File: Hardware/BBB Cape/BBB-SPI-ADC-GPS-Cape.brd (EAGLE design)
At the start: 72.1 x 86.3 mm, 8 parts

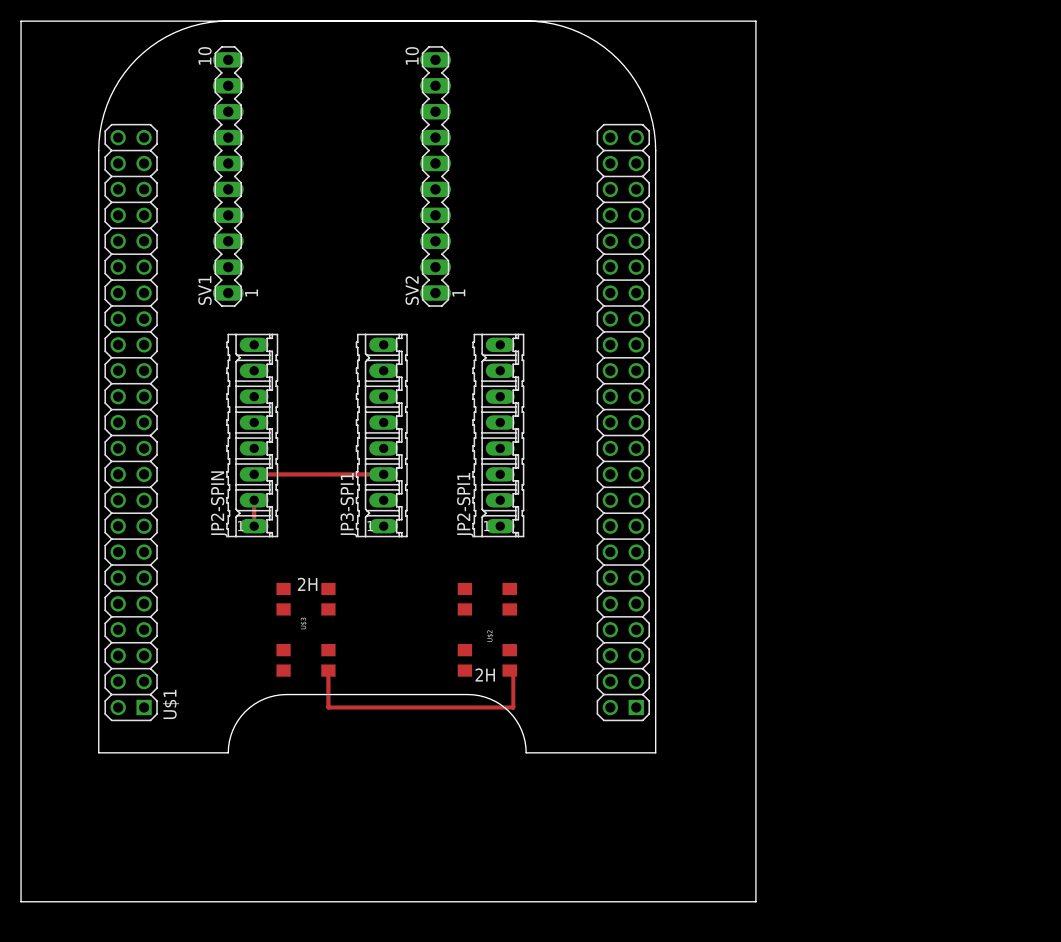
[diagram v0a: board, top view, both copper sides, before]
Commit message: Split cape into two components
Lower layer is the GPS and Pot and upper layer is the SPI connections
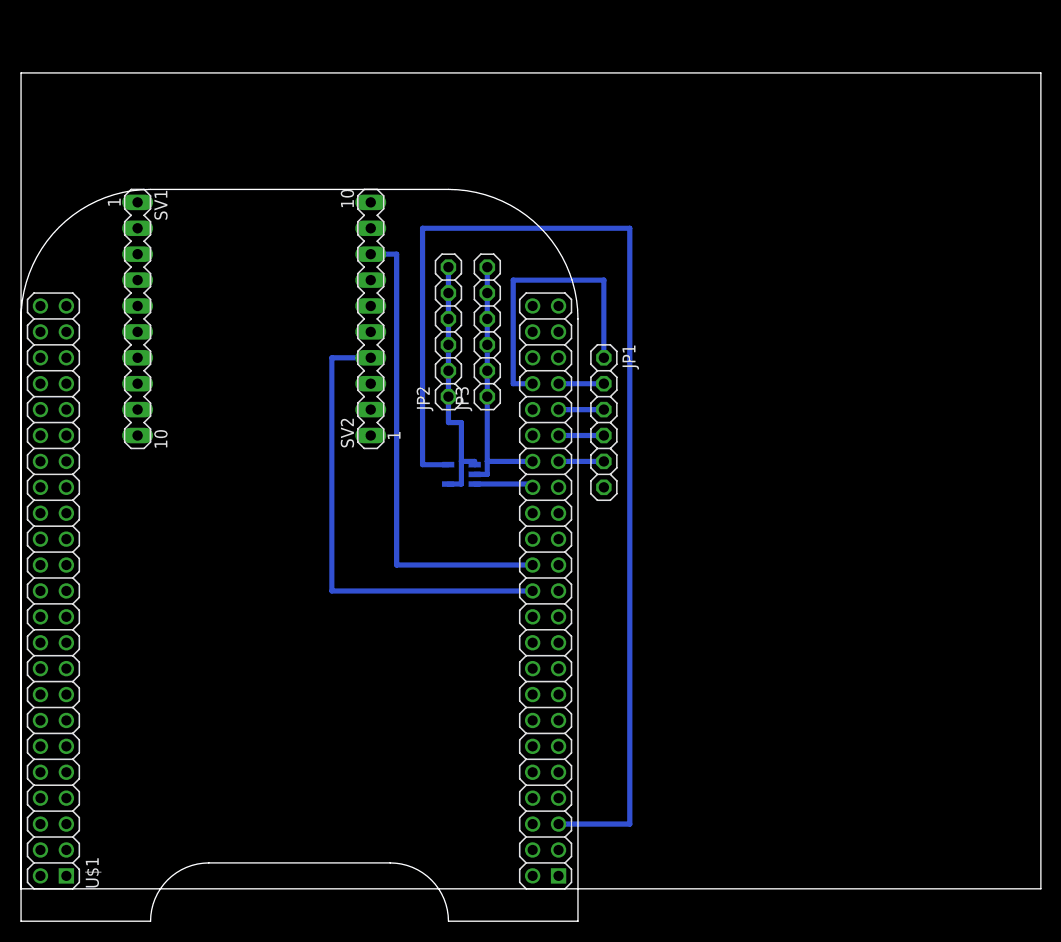
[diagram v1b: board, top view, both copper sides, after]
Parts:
- removed JP2-SPI1, JP2-SPIN, JP3-SPI1: (no value), con-amp-quick:08P
- removed U$2, U$3: CL-SB-23B-01TSMD, MADCAT-BBB-Cape:CL-SB-23B
- added JP1, JP2, JP3: (no value), adafruit:1X06
- added U$4: OPA344, SparkFun-AnalogIC:SOT23-5
- moved U$1 18.2 mm to (0.00, -17.8)
- moved SV1 16.6 mm to (11.4, 55.9), turned to 270 degrees
- moved SV2 15.3 mm to (34.3, 55.9)
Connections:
- removed net D: JP2-SPIN.3, JP3-SPI1.3, U$3.2
- removed net N$3: JP2-SPI1.8, U$2.6
- removed net VDD_3V3EXP: U$1.50
- new net AIN1: JP1.1, U$1.86
- new net AIN2: JP1.3, U$1.83
- new net AIN3: U$1.84
- new net AIN4: JP1.5, U$1.79
- new net AIN5: U$1.82
- new net AIN6: JP1.4, U$1.81
- new net GNDA_ADC: JP3.1, JP3.2, JP3.3, JP3.4, JP3.5, JP3.6, U$1.80, U$4.2
- new net N$2: JP2.1, JP2.2, JP2.3, JP2.4, JP2.5, JP2.6, U$4.1, U$4.4
- new net VDD_ADC: U$1.78, U$4.3
- net AIN0: now also JP1.2
- net CS: no longer JP2-SPI1.7, U$2.7
- net GND: no longer JP2-SPI1.1, JP2-SPI1.2, JP2-SPIN.1, JP2-SPIN.2, JP3-SPI1.2, U$2.8, U$3.1
- net SCL: no longer JP2-SPI1.6
- net SDA: no longer JP2-SPI1.5
- net SDO: no longer JP2-SPI1.4
- net VCC: now also U$1.50; no longer JP2-SPIN.8, JP3-SPI1.8, U$3.3
- net VDD_5V: now also U$4.5
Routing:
- net VDD_5V: track 0.00 -> 111.4 mm
- net TX-B: track 0.00 -> 46.4 mm
- net RX-B: track 0.00 -> 46.4 mm
- net AIN1: track 0.00 -> 28.6 mm
- net GND: track 28.2 -> 0.00 mm
- net GNDA_ADC: track 0.00 -> 26.0 mm
- net N$2: track 0.00 -> 25.5 mm
- net D: track 12.7 -> 0.00 mm
- net VDD_ADC: track 0.00 -> 6.00 mm
- net AIN6: track 0.00 -> 4.45 mm
- net AIN4: track 0.00 -> 4.45 mm
- net AIN2: track 0.00 -> 4.45 mm
- net AIN0: track 0.00 -> 4.45 mm
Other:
- board size 72.1 x 86.3 mm -> 100 x 80 mm
